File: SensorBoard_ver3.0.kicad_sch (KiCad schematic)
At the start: 45 parts, among them IC1 MIC5504-3.3YM5-T5, J1 STLink, SW1 CAN_Terminal, SW2 IDSetSW, SW3 Reset, SW4 IDSetSW, U1 L7805, U2 MAX3485, U3 ATA6561, U4 STM32F303K8Tx, Y1 Crystal

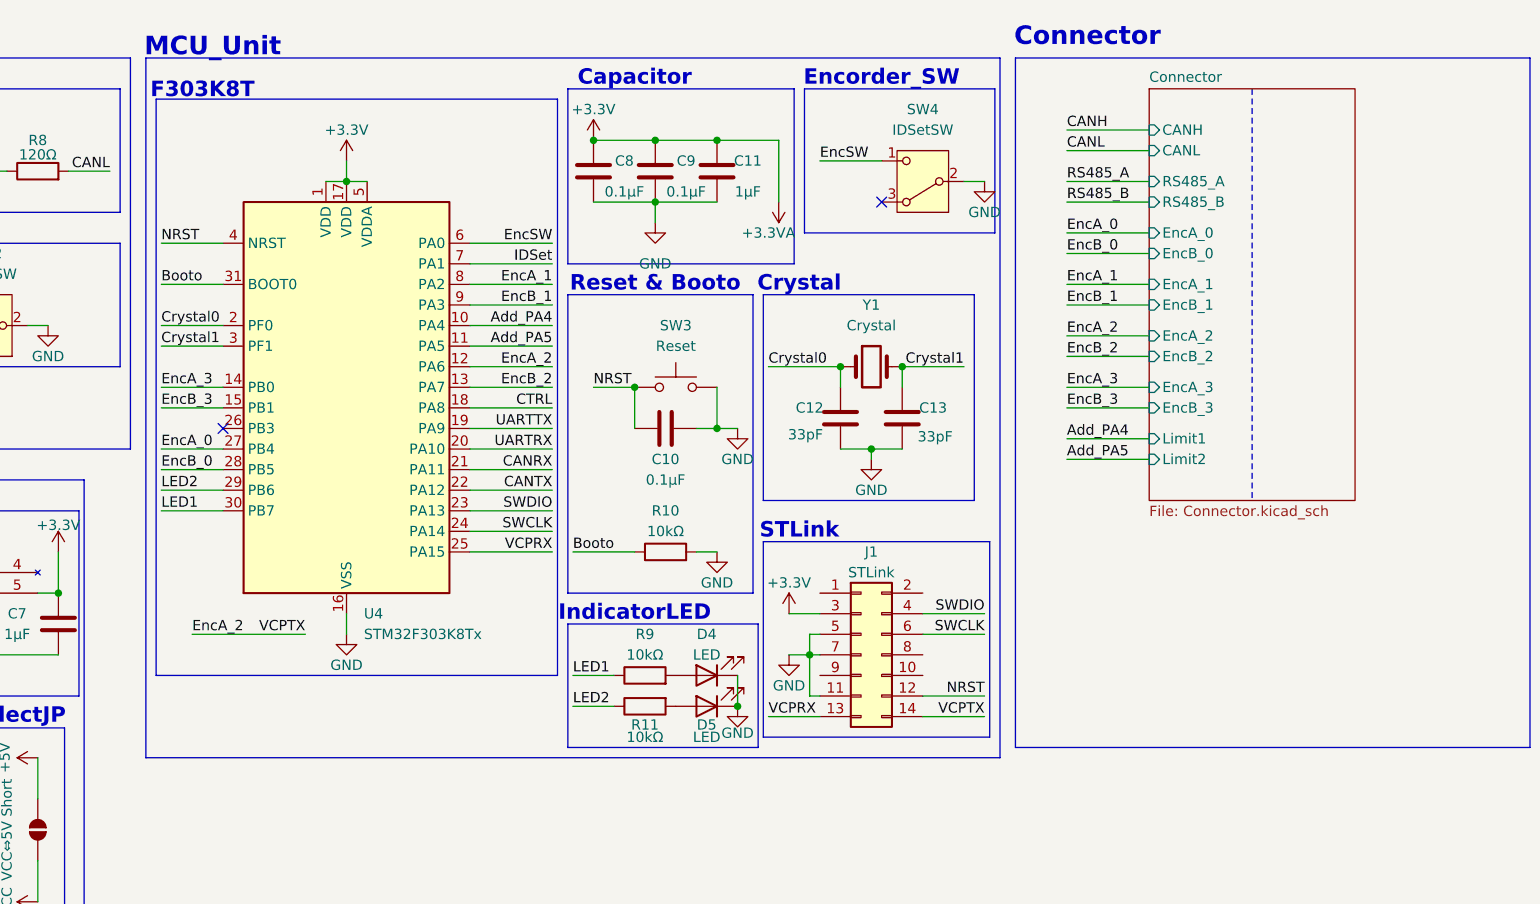
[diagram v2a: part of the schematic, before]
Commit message: ほとんど完成
残りすること
・終端抵抗の配線
・基板の見直し
・シルクの大型化
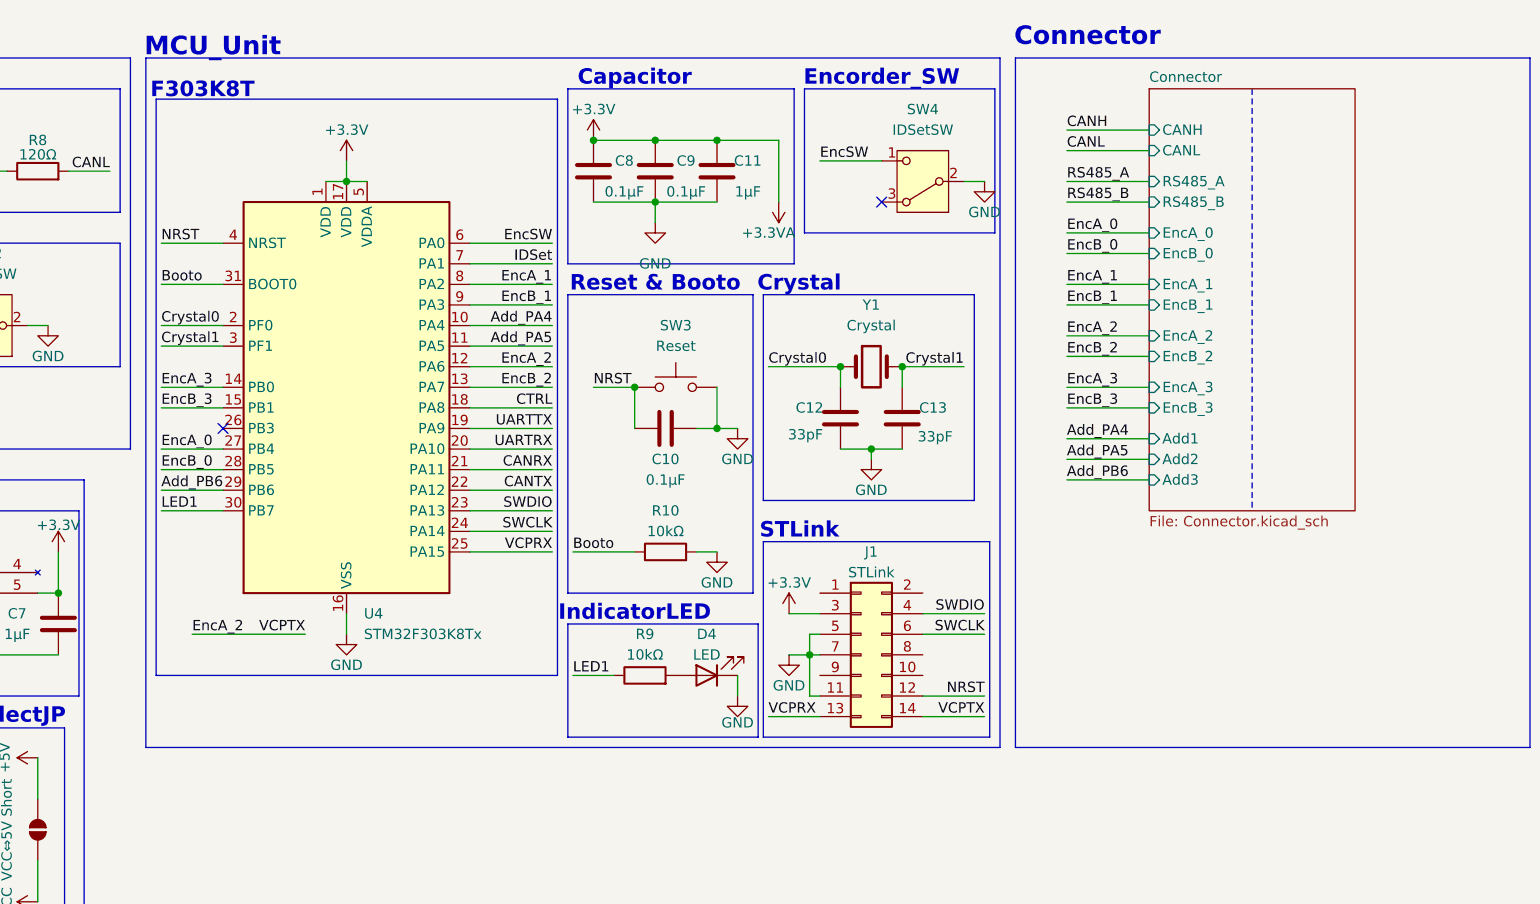
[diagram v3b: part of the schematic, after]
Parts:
- removed D5: LED, LED_SMD:LED_0603_1608Metric, symbol Device:LED
- removed R11: 10kΩ, Resistor_SMD:R_0603_1608Metric, symbol Device:R
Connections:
- net LED2 renamed Add_PB6
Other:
- sheet Connector ports: added Add1, Add2, Add3; removed Limit1, Limit2
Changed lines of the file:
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@@
 	(rectangle
 		(start 156.845 87.63)
-		(end 180.34 102.87)
+		(end 180.34 101.6)
 		(stroke
 			(width 0)
@@
 	(rectangle
 		(start 104.775 17.78)
-		(end 210.185 104.14)
+		(end 210.185 102.87)
 		(stroke
 			(width 0)
@@
 	)
 	(junction
-		(at 177.8 97.79)
-		(diameter 0)
-		(color 0 0 0 0)
-	)
-	(junction
 		(at 50.8 152.4)
 		(diameter 0)
@@
 	(wire
 		(pts
-			(xy 177.8 97.79) (xy 177.8 93.98)
+			(xy 177.8 96.52) (xy 177.8 93.98)
 		)
 		(stroke
@@
 	(wire
 		(pts
+			(xy 218.44 69.85) (xy 228.6 69.85)
+		)
+		(stroke
+			(width 0)
+			(type default)
+		)
+	)
+	(wire
+		(pts
 			(xy 144.78 40.64) (xy 154.94 40.64)
 		)
@@
 	(wire
 		(pts
-			(xy 157.48 97.79) (xy 162.56 97.79)
-		)
-		(stroke
-			(width 0)
-			(type default)
-		)
-	)
-	(wire
-		(pts
 			(xy 22.86 91.44) (xy 33.02 91.44)
 		)
@@
 	(polyline
 		(pts
-			(xy 241.3 21.59) (xy 241.3 72.39)
+			(xy 241.3 21.59) (xy 241.3 73.66)
 		)
 		(stroke
@@
 		)
 	)
+	(label "Add_PB6"
+		(at 218.44 69.85 0)
+		(effects
+			(font
+				(size 1.27 1.27)
+			)
+			(justify left bottom)
+		)
+	)
 	(label "RS485_A"
 		(at 62.865 144.78 180)
@@
 		)
 	)
-	(label "LED2"
+	(label "Add_PB6"
 		(at 106.68 71.12 0)
 		(effects
@@
 		)
 	)
-	(label "LED2"
-		(at 157.48 97.79 0)
-		(effects
-			(font
-				(size 1.27 1.27)
-			)
-			(justify left bottom)
-		)
-	)
 	(label "VCPTX"
 		(at 208.28 99.06 180)
@@
 	)
 	(symbol
-		(lib_id "Device:R")
-		(at 166.37 97.79 90)
-		(mirror x)
-		(unit 1)
-		(exclude_from_sim no)
-		(in_bom yes)
-		(on_board yes)
-		(dnp no)
-		(property "Reference" "R11"
-			(at 166.37 100.076 90)
-			(effects
-				(font
-					(size 1.27 1.27)
-				)
-			)
-		)
-		(property "Value" "10kΩ"
-			(at 166.37 101.6 90)
-			(effects
-				(font
-					(size 1.27 1.27)
-				)
-			)
-		)
-		(property "Footprint" "Resistor_SMD:R_0603_1608Metric"
-			(at 166.37 96.012 90)
-			(effects
-				(font
-					(size 1.27 1.27)
-				)
-				(hide yes)
-			)
-		)
-		(property "Datasheet" "~"
-			(at 166.37 97.79 0)
-			(effects
-				(font
-					(size 1.27 1.27)
-				)
-				(hide yes)
-			)
-		)
-		(property "Description" "Resistor"
-			(at 166.37 97.79 0)
-			(effects
-				(font
-					(size 1.27 1.27)
-				)
-				(hide yes)
-			)
-		)
-		(pin "1"
-		)
-		(pin "2"
-		)
-		(instances
-			(project "SensorBoard_ver3.0"
-				(path "/48207ddc-a67e-4dc5-8222-aef69eda58f7"
-					(reference "R11")
-					(unit 1)
-				)
-			)
-		)
-	)
-	(symbol
 		(lib_id "Device:C")
 		(at 49.53 58.42 90)
@@
 	)
 	(symbol
-		(lib_id "Device:LED")
-		(at 173.99 97.79 180)
-		(unit 1)
-		(exclude_from_sim no)
-		(in_bom yes)
-		(on_board yes)
-		(dnp no)
-		(property "Reference" "D5"
-			(at 173.99 100.076 0)
-			(effects
-				(font
-					(size 1.27 1.27)
-				)
-			)
-		)
-		(property "Value" "LED"
-			(at 173.99 101.6 0)
-			(effects
-				(font
-					(size 1.27 1.27)
-				)
-			)
-		)
-		(property "Footprint" "LED_SMD:LED_0603_1608Metric"
-			(at 173.99 97.79 0)
-			(effects
-				(font
-					(size 1.27 1.27)
-				)
-				(hide yes)
-			)
-		)
-		(property "Datasheet" "~"
-			(at 173.99 97.79 0)
-			(effects
-				(font
-					(size 1.27 1.27)
-				)
-				(hide yes)
-			)
-		)
-		(property "Description" "Light emitting diode"
-			(at 173.99 97.79 0)
-			(effects
-				(font
-					(size 1.27 1.27)
-				)
-				(hide yes)
-			)
-		)
-		(property "Sim.Pins" "1=K 2=A"
-			(at 173.99 97.79 0)
-			(effects
-				(font
-					(size 1.27 1.27)
-				)
-				(hide yes)
-			)
-		)
-		(pin "1"
-		)
-		(pin "2"
-		)
-		(instances
-			(project "SensorBoard_ver3.0"
-				(path "/48207ddc-a67e-4dc5-8222-aef69eda58f7"
-					(reference "D5")
-					(unit 1)
-				)
-			)
-		)
-	)
-	(symbol
 		(lib_id "Device:C")
 		(at 198.12 62.23 0)
@@
 	(symbol
 		(lib_id "power:GND")
-		(at 177.8 97.79 0)
+		(at 177.8 96.52 0)
 		(unit 1)
 		(exclude_from_sim no)
@@
 		(dnp no)
 		(property "Reference" "#PWR032"
-			(at 177.8 104.14 0)
+			(at 177.8 102.87 0)
 			(effects
 				(font
@@
 		)
 		(property "Value" "GND"
-			(at 177.8 101.092 0)
+			(at 177.8 99.822 0)
 			(effects
 				(font
@@
 		)
 		(property "Footprint" ""
-			(at 177.8 97.79 0)
+			(at 177.8 96.52 0)
 			(effects
 				(font
@@
 		)
 		(property "Datasheet" ""
-			(at 177.8 97.79 0)
+			(at 177.8 96.52 0)
 			(effects
 				(font
@@
 		)
 		(property "Description" "Power symbol creates a global label with name \"GND\" , ground"
-			(at 177.8 97.79 0)
+			(at 177.8 96.52 0)
 			(effects
 				(font
@@
 	(sheet
 		(at 228.6 21.59)
-		(size 25.4 50.8)
+		(size 25.4 52.07)
 		(exclude_from_sim no)
 		(in_bom yes)
@@
 		)
 		(property "Sheetfile" "Connector.kicad_sch"
-			(at 228.6 72.9746 0)
+			(at 228.6 74.2446 0)
 			(effects
 				(font
@@
 			)
 		)
-		(pin "Limit1" input
+		(pin "Add1" input
 			(at 228.6 64.77 180)
 			(effects
@@
 			)
 		)
-		(pin "Limit2" input
+		(pin "Add2" input
 			(at 228.6 67.31 180)
 			(effects
 				(font
+					(size 1.27 1.27)
+				)
+				(justify left)
+			)
+		)
+		(pin "Add3" input
+			(at 228.6 69.85 180)
+			(effects
+				(font

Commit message: ほとんど完成
再チェックして、発注したい
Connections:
- net EncA_1: now also J1.14 (Pin_14)
- net EncA_2: no longer J1.14 (Pin_14)
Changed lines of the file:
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@@
 	(rectangle
 		(start 212.09 17.78)
-		(end 275.59 102.87)
+		(end 256.54 77.47)
 		(stroke
 			(width 0)
@@
 	(text "Connector"
 		(exclude_from_sim no)
-		(at 220.98 15.24 0)
+		(at 220.98 16.256 0)
 		(effects
 			(font
@@
 		)
 	)
-	(polyline
-		(pts
-			(xy 241.3 21.59) (xy 241.3 73.66)
-		)
-		(stroke
-			(width 0)
-			(type dash_dot)
-			(color 132 0 0 1)
-		)
-	)
 	(wire
 		(pts
@@
 		)
 	)
-	(label "EncA_2"
+	(label "EncA_1"
 		(at 110.49 88.9 0)
 		(effects

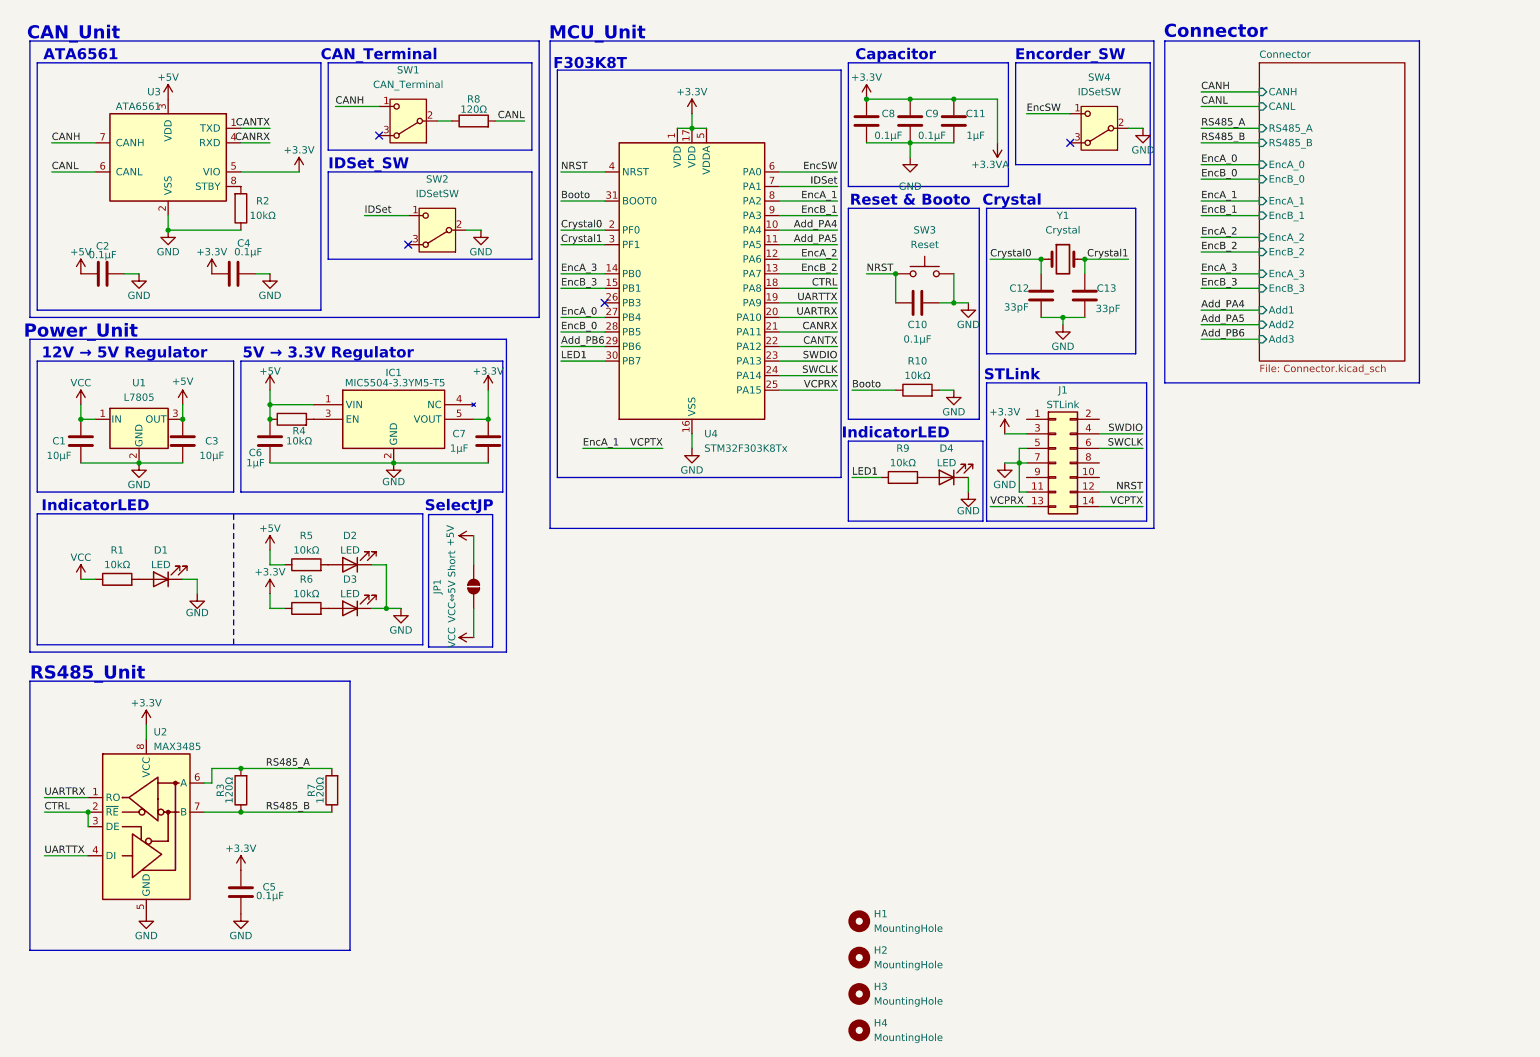
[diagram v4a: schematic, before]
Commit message: いろいろ修正
・フェライトビーズの追加
・シルクの追加
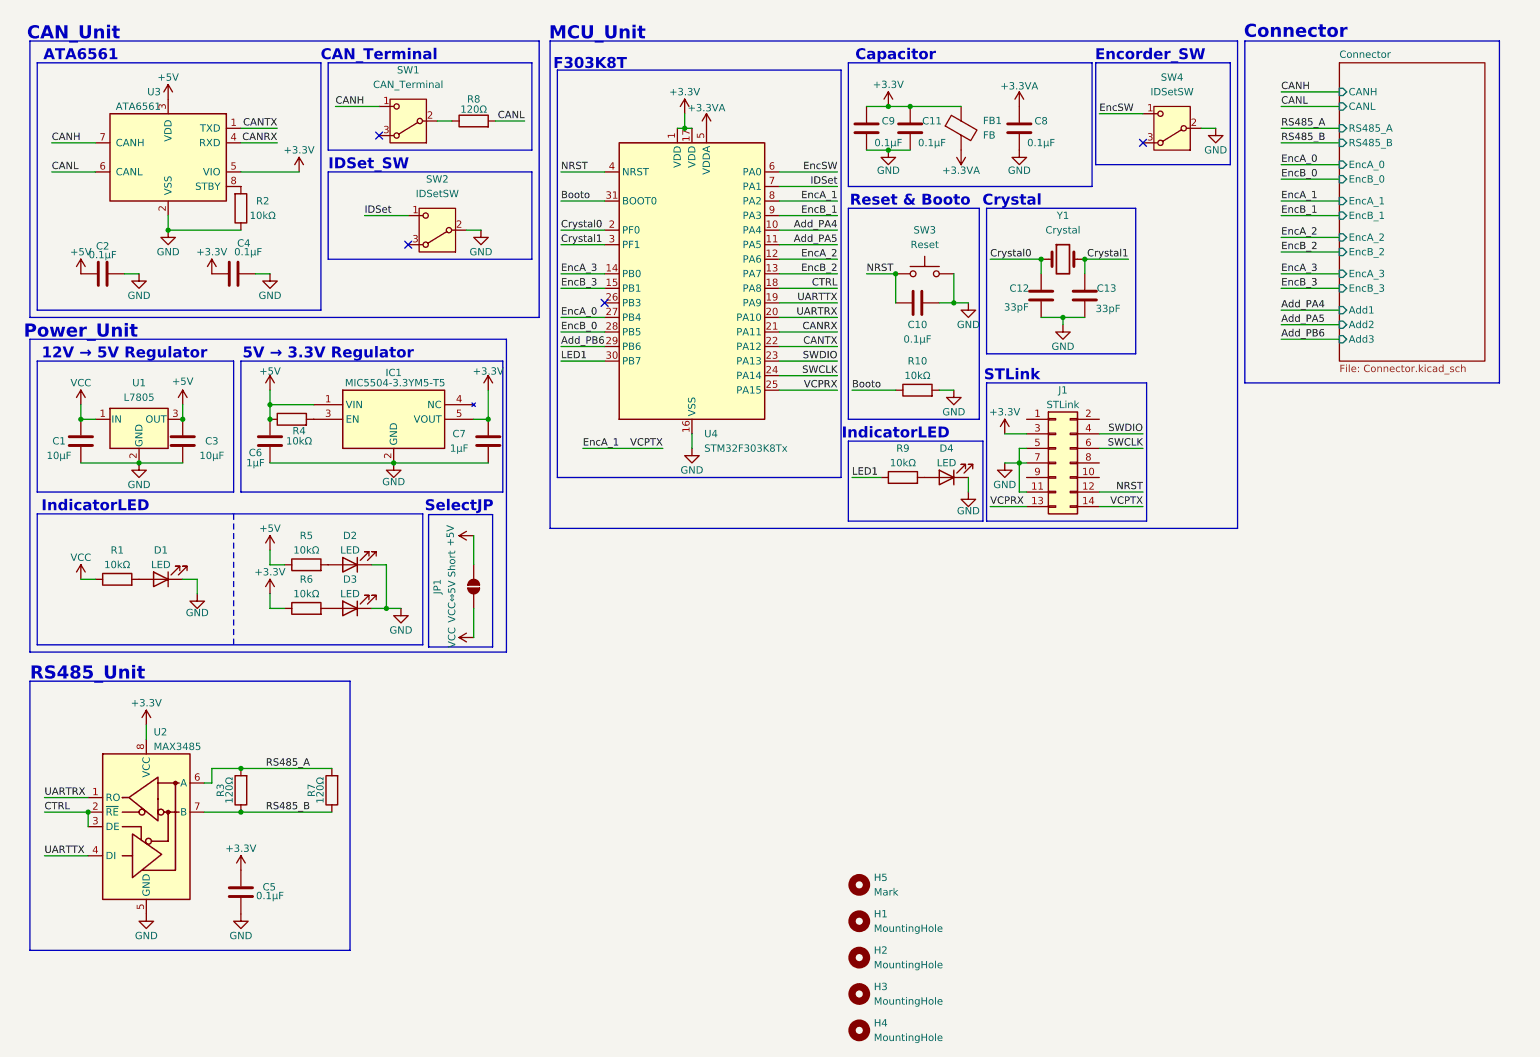
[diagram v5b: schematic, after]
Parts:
- added FB1: FB, Inductor_SMD:L_0603_1608Metric, symbol Device:FerriteBead
- added H5: Mark, SensorBoard_ver3.0:α-LumiCode, symbol Mechanical:MountingHole
- C11: value 1μF -> 0.1μF
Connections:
- net +3.3V: now also FB1.1; no longer C8.1, U4.5 (VDDA)
- new net +3.3VA: C8.1, FB1.2, U4.5 (VDDA)
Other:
- moved on the sheet: C11, C8, C9, SW4
